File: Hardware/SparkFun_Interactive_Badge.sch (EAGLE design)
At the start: 1 part

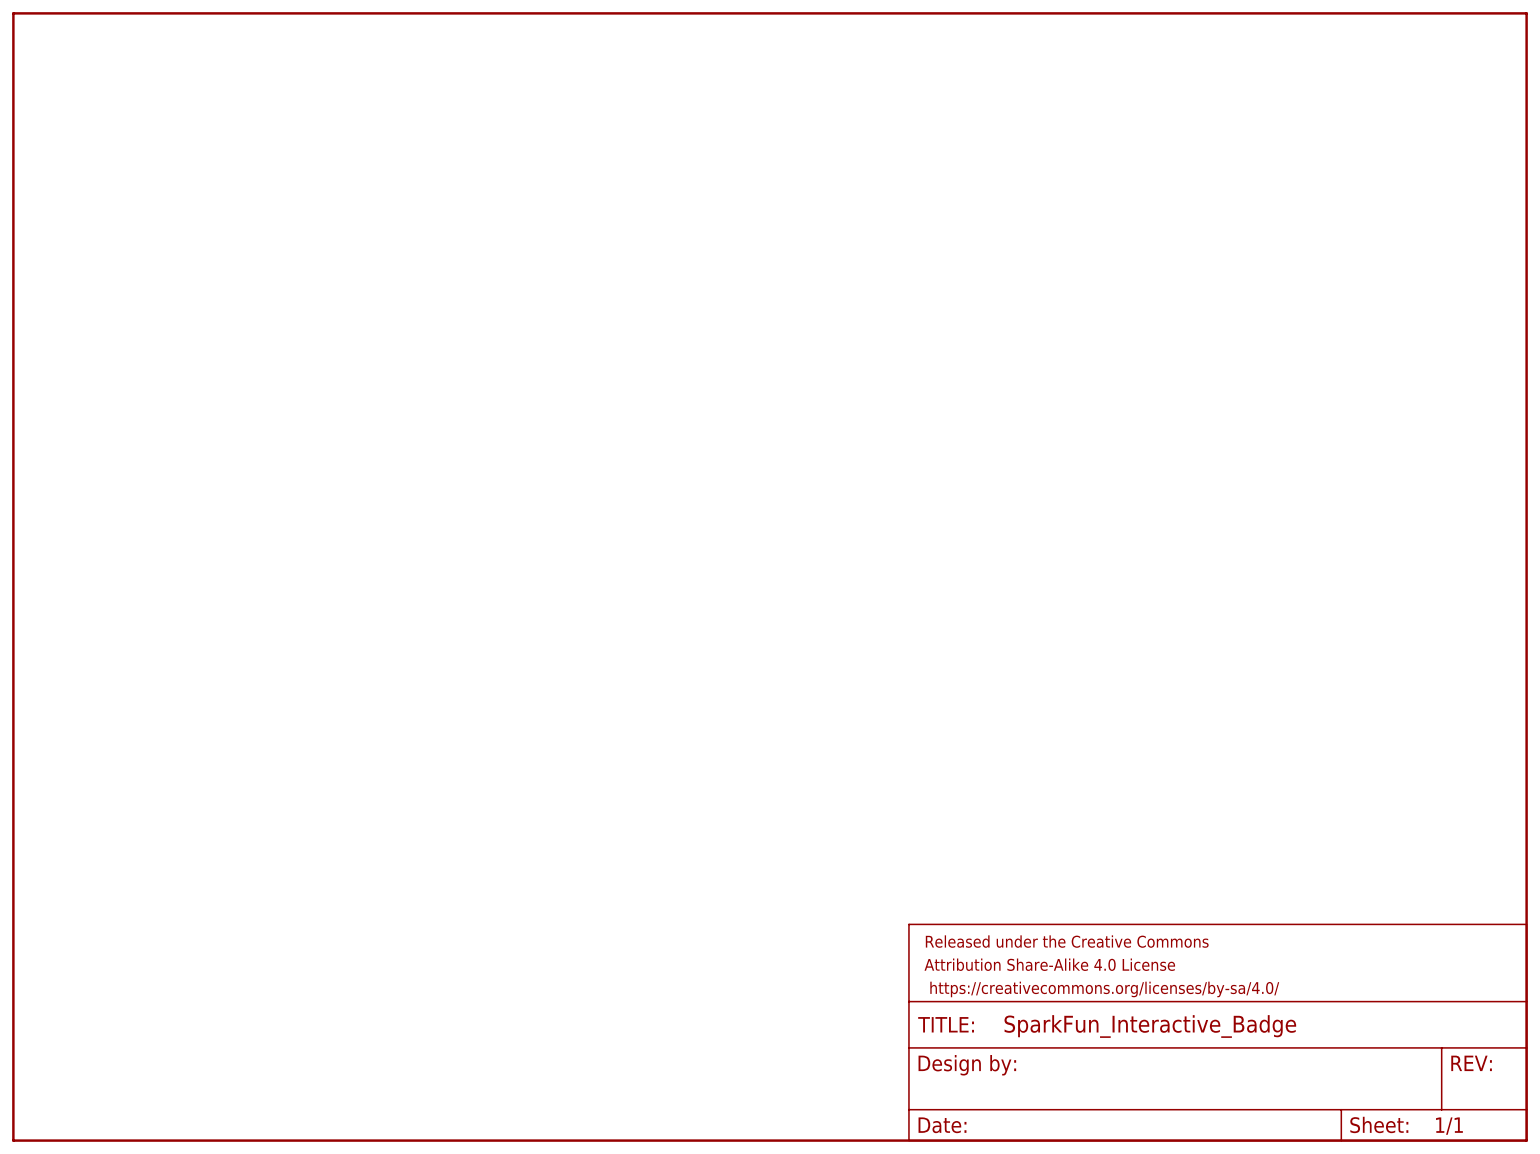
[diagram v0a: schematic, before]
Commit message: Started schematic. Voltage selection circuit added.
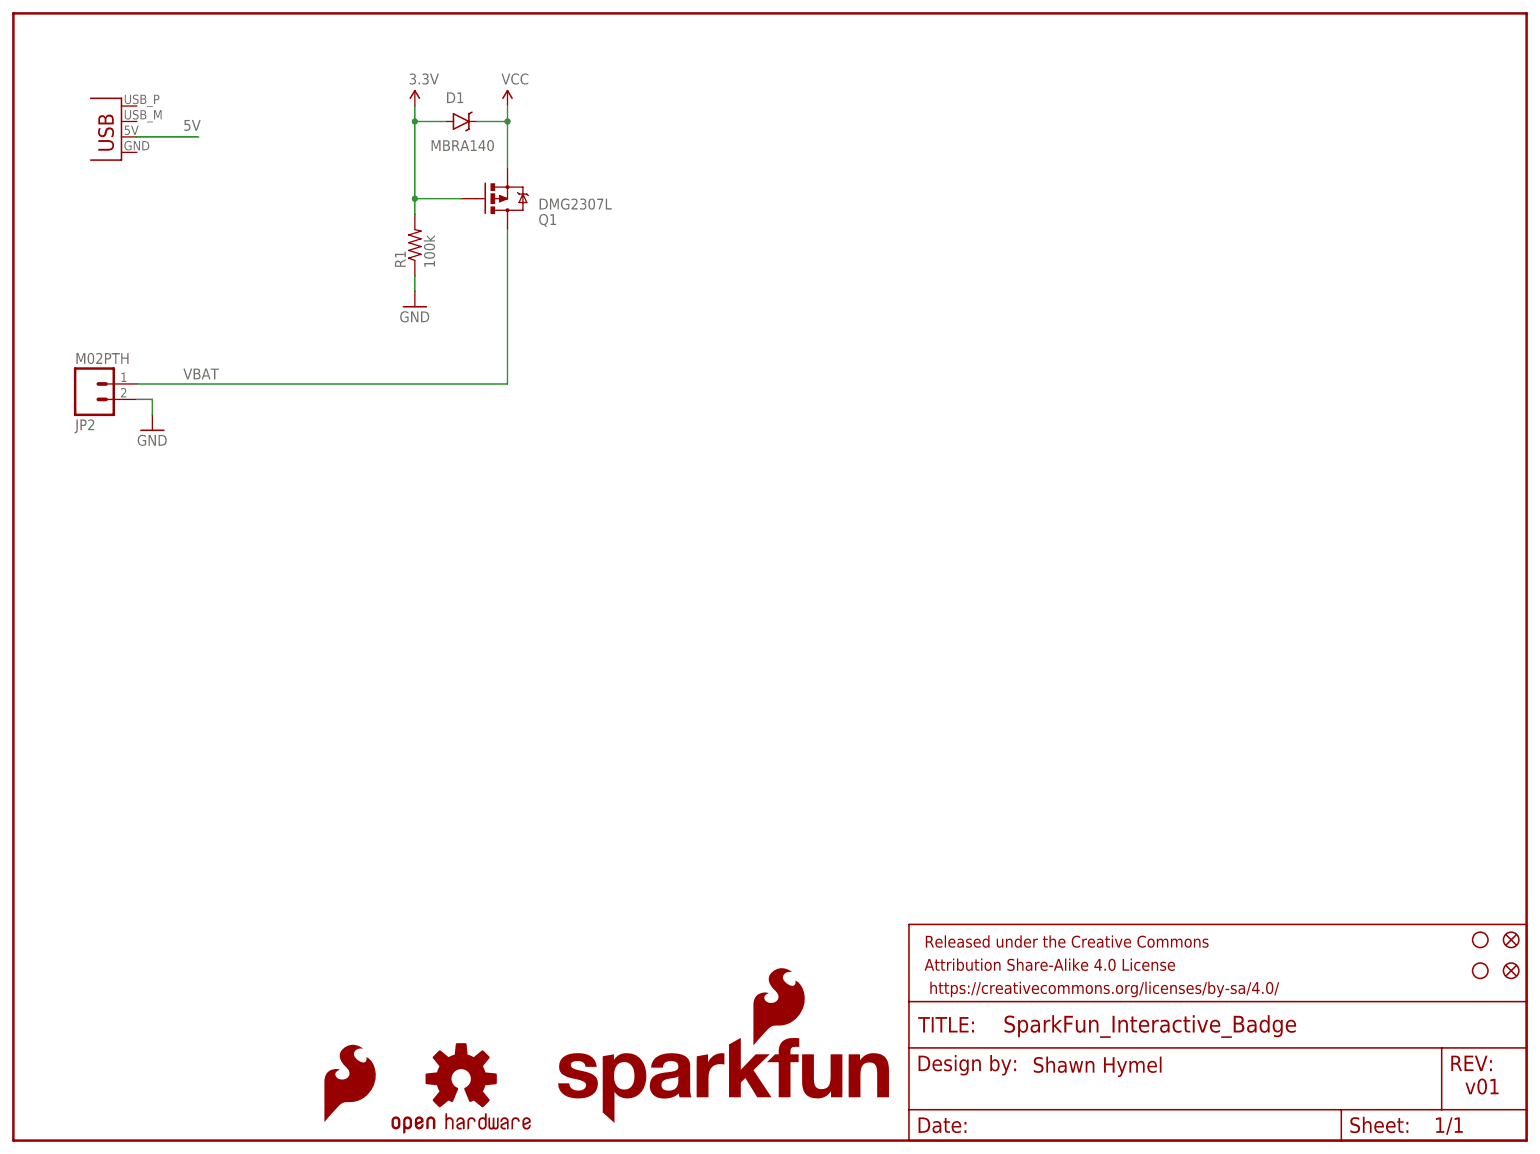
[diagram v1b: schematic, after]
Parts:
- added D1: MBRA140, SparkFun-DiscreteSemi:DIODE-SCHOTTKY-MBRA140
- added FID1, FID2: FIDUCIAL1X2, SparkFun-Aesthetics:FIDUCIAL1X2
- added JP1: USBPCB, SparkFun-Connectors:USBPCB
- added JP2: M02PTH, SparkFun-Connectors:M02PTH
- added LOGO1: SFE_LOGO_FLAME.1_INCH, SparkFun-Aesthetics:SFE_LOGO_FLAME.1_INCH
- added LOGO2: OSHW-LOGOS, SparkFun-Aesthetics:OSHW-LOGOS
- added Q1: DMG2307L, SparkFun-DiscreteSemi:MOSFET-PCHANNELDMG2307L
- added R1: 100k, SparkFun-Resistors:100KOHM1/10W1%(0603)
- added STANDOFF1, STANDOFF2: STAND-OFF, SparkFun-Electromechanical:STAND-OFF
- added U$1: SFE_LOGO_NAME_FLAME.1_INCH, SparkFun-Aesthetics:SFE_LOGO_NAME_FLAME.1_INCH
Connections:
- new net 3.3V: D1.A, Q1.G, R1.2
- new net 5V: JP1.VBUS
- new net GND: JP2.2, R1.1
- new net VBAT: JP2.1, Q1.D
- new net VCC: D1.C, Q1.S
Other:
- note added: "Shawn Hymel"
- note added: "v01"
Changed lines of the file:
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@@
 <setting verticaltext="up"/>
 </settings>
-<grid distance="0.1" unitdist="inch" unit="inch" style="lines" multiple="1" display="no" altdistance="0.01" altunitdist="inch" altunit="inch"/>
+<grid distance="0.1" unitdist="inch" unit="inch" style="lines" multiple="1" display="yes" altdistance="0.01" altunitdist="inch" altunit="inch"/>
 <layers>
 <layer number="1" name="Top" color="4" fill="1" visible="no" active="no"/>
@@
 <layer number="54" name="bGND_GNDA" color="1" fill="9" visible="no" active="no"/>
 <layer number="56" name="wert" color="7" fill="1" visible="no" active="no"/>
+<layer number="57" name="tCAD" color="7" fill="1" visible="no" active="no"/>
 <layer number="90" name="Modules" color="5" fill="1" visible="yes" active="yes"/>
 <layer number="91" name="Nets" color="2" fill="1" visible="yes" active="yes"/>
@@
 <layer number="97" name="Info" color="7" fill="1" visible="yes" active="yes"/>
 <layer number="98" name="Guide" color="6" fill="1" visible="yes" active="yes"/>
+<layer number="99" name="SpiceOrder" color="7" fill="1" visible="yes" active="yes"/>
 <layer number="100" name="Muster" color="7" fill="1" visible="no" active="no"/>
 <layer number="101" name="Patch_Top" color="12" fill="4" visible="yes" active="yes"/>
@@
 <layer number="108" name="tplace-old" color="10" fill="1" visible="no" active="yes"/>
 <layer number="109" name="ref-old" color="11" fill="1" visible="no" active="yes"/>
+<layer number="110" name="fp0" color="7" fill="1" visible="yes" active="yes"/>
+<layer number="111" name="LPC17xx" color="7" fill="1" visible="yes" active="yes"/>
+<layer number="112" name="tSilk" color="7" fill="1" visible="yes" active="yes"/>
+<layer number="113" name="IDFDebug" color="4" fill="1" visible="yes" active="yes"/>
 <layer number="116" name="Patch_BOT" color="9" fill="4" visible="yes" active="yes"/>
 <layer number="121" name="_tsilk" color="7" fill="1" visible="yes" active="yes"/>
 <layer number="122" name="_bsilk" color="7" fill="1" visible="yes" active="yes"/>
+<layer number="123" name="tTestmark" color="7" fill="1" visible="yes" active="yes"/>
+<layer number="124" name="bTestmark" color="7" fill="1" visible="yes" active="yes"/>
 <layer number="125" name="_tNames" color="7" fill="1" visible="yes" active="yes"/>
+<layer number="126" name="_bNames" color="7" fill="1" visible="yes" active="yes"/>
+<layer number="127" name="_tValues" color="7" fill="1" visible="yes" active="yes"/>
+<layer number="128" name="_bValues" color="7" fill="1" visible="yes" active="yes"/>
+<layer number="131" name="tAdjust" color="7" fill="1" visible="yes" active="yes"/>
+<layer number="132" name="bAdjust" color="7" fill="1" visible="yes" active="yes"/>
 <layer number="144" name="Drill_legend" color="7" fill="1" visible="yes" active="yes"/>
+<layer number="150" name="Notes" color="7" fill="1" visible="yes" active="yes"/>
 <layer number="151" name="HeatSink" color="7" fill="1" visible="yes" active="yes"/>
+<layer number="152" name="_bDocu" color="7" fill="1" visible="yes" active="yes"/>
+<layer number="153" name="FabDoc1" color="7" fill="1" visible="yes" active="yes"/>
+<layer number="154" name="FabDoc2" color="7" fill="1" visible="yes" active="yes"/>
+<layer number="155" name="FabDoc3" color="7" fill="1" visible="yes" active="yes"/>
 <layer number="199" name="Contour" color="7" fill="1" visible="yes" active="yes"/>
 <layer number="200" name="200bmp" color="1" fill="10" visible="yes" active="yes"/>
@@
 <layer number="223" name="223bmp" color="24" fill="1" visible="no" active="no"/>
 <layer number="224" name="224bmp" color="25" fill="1" visible="no" active="no"/>
+<layer number="248" name="Housing" color="7" fill="1" visible="yes" active="yes"/>
+<layer number="249" name="Edge" color="7" fill="1" visible="yes" active="yes"/>
 <layer number="250" name="Descript" color="3" fill="1" visible="no" active="no"/>
 <layer number="251" name="SMDround" color="12" fill="11" visible="no" active="no"/>
 <layer number="254" name="cooling" color="7" fill="1" visible="yes" active="yes"/>
+<layer number="255" name="routoute" color="7" fill="1" visible="no" active="yes"/>
 </layers>
 <schematic xreflabel="%F%N/%S" xrefpart="1_/%S.%C%R">
@@
 <parts>
 <part name="FRAME1" library="SparkFun-Aesthetics" deviceset="FRAME-LETTER" device=""/>
+<part name="FID1" library="SparkFun-Aesthetics" deviceset="FIDUCIAL" device="1X2"/>
+<part name="FID2" library="SparkFun-Aesthetics" deviceset="FIDUCIAL" device="1X2"/>
+<part name="STANDOFF1" library="SparkFun-Electromechanical" deviceset="STAND-OFF" device=""/>
+<part name="STANDOFF2" library="SparkFun-Electromechanical" deviceset="STAND-OFF" device=""/>
+<part name="LOGO1" library="SparkFun-Aesthetics" deviceset="SFE_LOGO_FLAME" device=".1_INCH"/>
+<part name="LOGO2" library="SparkFun-Aesthetics" deviceset="OSHW-LOGO" device="S"/>
+<part name="U$1" library="SparkFun-Aesthetics" deviceset="SFE_LOGO_NAME_FLAME" device=".1_INCH"/>
+<part name="JP1" library="SparkFun-Connectors" deviceset="USB" device="PCB"/>
+<part name="Q1" library="SparkFun-DiscreteSemi" deviceset="MOSFET-PCHANNEL" device="DMG2307L" value="DMG2307L"/>
+<part name="R1" library="SparkFun-Resistors" deviceset="100KOHM1/10W1%(0603)" device="" value="100k"/>
+<part name="D1" library="SparkFun-DiscreteSemi" deviceset="DIODE-SCHOTTKY" device="-MBRA140" value="MBRA140"/>
+<part name="GND15" library="SparkFun-Aesthetics" deviceset="GND" device=""/>
+<part name="SUPPLY1" library="SparkFun-Aesthetics" deviceset="VCC" device=""/>
+<part name="JP2" library="SparkFun-Connectors" deviceset="M02" device="PTH"/>
+<part name="GND1" library="SparkFun-Aesthetics" deviceset="GND" device=""/>
+<part name="SUPPLY2" library="SparkFun-Aesthetics" deviceset="3.3V" device=""/>
 </parts>
 <sheets>
 <sheet>
 <plain>
+<text x="238.76" y="7.62" size="2.54" layer="94">v01</text>
+<text x="167.64" y="11.176" size="2.54" layer="94">Shawn Hymel</text>
 </plain>
 <instances>
 <instance part="FRAME1" gate="G$1" x="0" y="0"/>
 <instance part="FRAME1" gate="G$2" x="147.32" y="0"/>
+<instance part="FID1" gate="G$1" x="246.38" y="33.02"/>
+<instance part="FID2" gate="G$1" x="246.38" y="27.94"/>
+<instance part="STANDOFF1" gate="G$1" x="241.3" y="33.02"/>
+<instance part="STANDOFF2" gate="G$1" x="241.3" y="27.94"/>
+<instance part="LOGO1" gate="G$1" x="50.8" y="2.54"/>
+<instance part="LOGO2" gate="G$1" x="73.66" y="10.16"/>
+<instance part="U$1" gate="G$1" x="88.9" y="2.54"/>
+<instance part="JP1" gate="G$1" x="17.78" y="162.56" rot="MR0"/>
+<instance part="Q1" gate="G$1" x="81.28" y="154.94" rot="MR180"/>
+<instance part="R1" gate="G$1" x="66.04" y="147.32" rot="R90"/>
+<instance part="D1" gate="G$1" x="73.66" y="167.64" smashed="yes">
+<attribute name="NAME" x="71.12" y="170.6626" size="1.778" layer="95"/>
+<attribute name="VALUE" x="68.58" y="162.7886" size="1.778" layer="96"/>
+</instance>
+<instance part="GND15" gate="1" x="66.04" y="137.16"/>
+<instance part="SUPPLY1" gate="G$1" x="81.28" y="170.18"/>
+<instance part="JP2" gate="G$1" x="12.7" y="124.46" rot="MR180"/>
+<instance part="GND1" gate="1" x="22.86" y="116.84"/>
+<instance part="SUPPLY2" gate="G$1" x="66.04" y="170.18"/>
 </instances>
 <busses>
 </busses>
 <nets>
+<net name="GND" class="0">
+<segment>
+<pinref part="R1" gate="G$1" pin="1"/>
+<pinref part="GND15" gate="1" pin="GND"/>
+<wire x1="66.04" y1="142.24" x2="66.04" y2="139.7" width="0.1524" layer="91"/>
+</segment>
+<segment>
+<pinref part="JP2" gate="G$1" pin="2"/>
+<wire x1="20.32" y1="121.92" x2="22.86" y2="121.92" width="0.1524" layer="91"/>
+<pinref part="GND1" gate="1" pin="GND"/>
+<wire x1="22.86" y1="121.92" x2="22.86" y2="119.38" width="0.1524" layer="91"/>
+</segment>
+</net>
+<net name="VBAT" class="0">
+<segment>
+<pinref part="Q1" gate="G$1" pin="D"/>
+<wire x1="20.32" y1="124.46" x2="81.28" y2="124.46" width="0.1524" layer="91"/>
+<wire x1="81.28" y1="124.46" x2="81.28" y2="149.86" width="0.1524" layer="91"/>
+<pinref part="JP2" gate="G$1" pin="1"/>
+<label x="27.94" y="125.222" size="1.778" layer="95"/>
+</segment>
+</net>
+<net name="VCC" class="0">
+<segment>
+<pinref part="D1" gate="G$1" pin="C"/>
+<wire x1="76.2" y1="167.64" x2="81.28" y2="167.64" width="0.1524" layer="91"/>
+<wire x1="81.28" y1="167.64" x2="81.28" y2="170.18" width="0.1524" layer="91"/>
+<pinref part="Q1" gate="G$1" pin="S"/>
+<wire x1="81.28" y1="167.64" x2="81.28" y2="160.02" width="0.1524" layer="91"/>
+<junction x="81.28" y="167.64"/>
+<pinref part="SUPPLY1" gate="G$1" pin="VCC"/>
+</segment>
+</net>
+<net name="3.3V" class="0">
+<segment>
+<pinref part="D1" gate="G$1" pin="A"/>
+<pinref part="R1" gate="G$1" pin="2"/>
+<wire x1="66.04" y1="167.64" x2="71.12" y2="167.64" width="0.1524" layer="91"/>
+<wire x1="66.04" y1="152.4" x2="66.04" y2="154.94" width="0.1524" layer="91"/>
+<pinref part="Q1" gate="G$1" pin="G"/>
+<wire x1="66.04" y1="154.94" x2="66.04" y2="167.64" width="0.1524" layer="91"/>
+<wire x1="73.66" y1="154.94" x2="66.04" y2="154.94" width="0.1524" layer="91"/>
+<junction x="66.04" y="154.94"/>
+<wire x1="66.04" y1="167.64" x2="66.04" y2="170.18" width="0.1524" layer="91"/>
+<junction x="66.04" y="167.64"/>
+<pinref part="SUPPLY2" gate="G$1" pin="3.3V"/>
+</segment>
+</net>
+<net name="5V" class="0">
+<segment>
+<pinref part="JP1" gate="G$1" pin="VBUS"/>
+<wire x1="20.32" y1="165.1" x2="30.48" y2="165.1" width="0.1524" layer="91"/>
+<label x="27.94" y="166.116" size="1.778" layer="95"/>
+</segment>
+</net>
 </nets>
 </sheet>

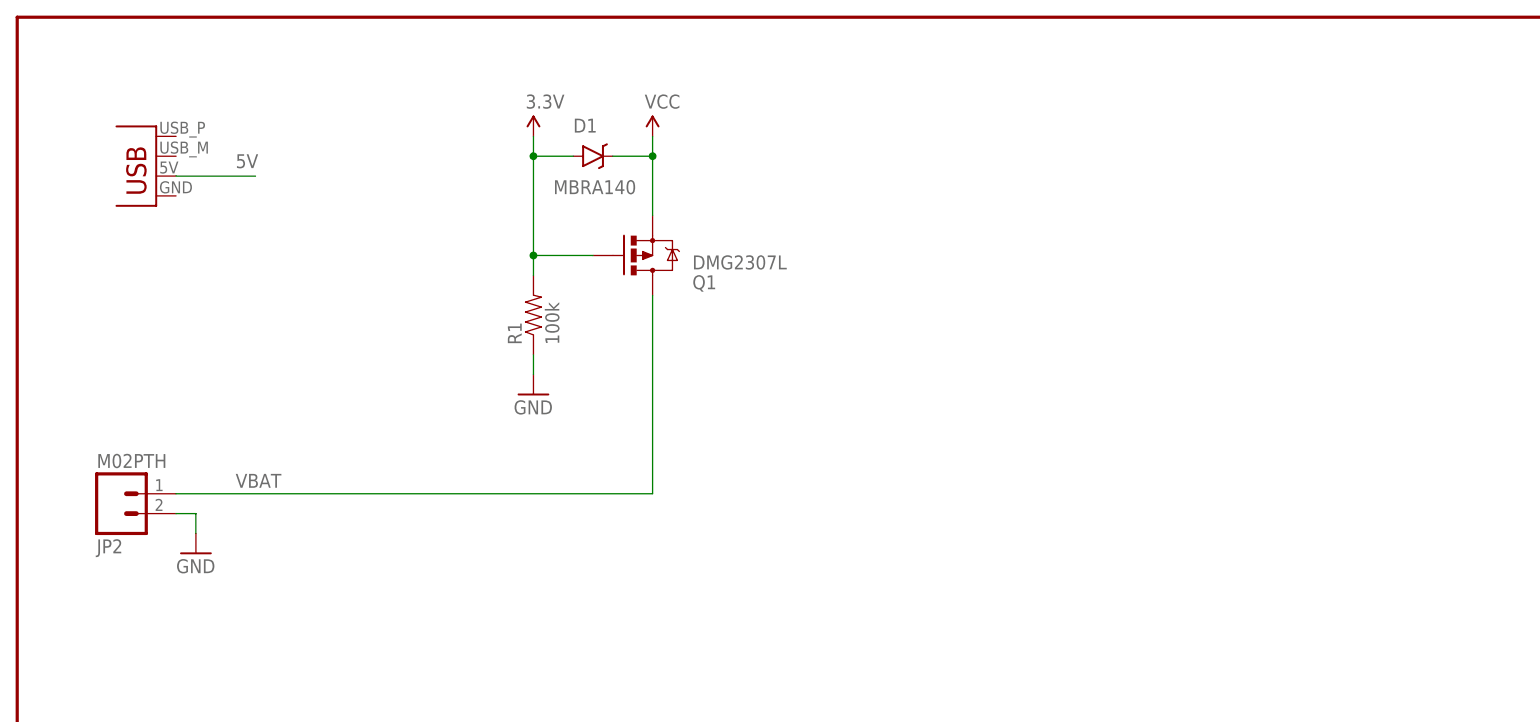
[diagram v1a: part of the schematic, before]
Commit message: Added LDO to power section in sch
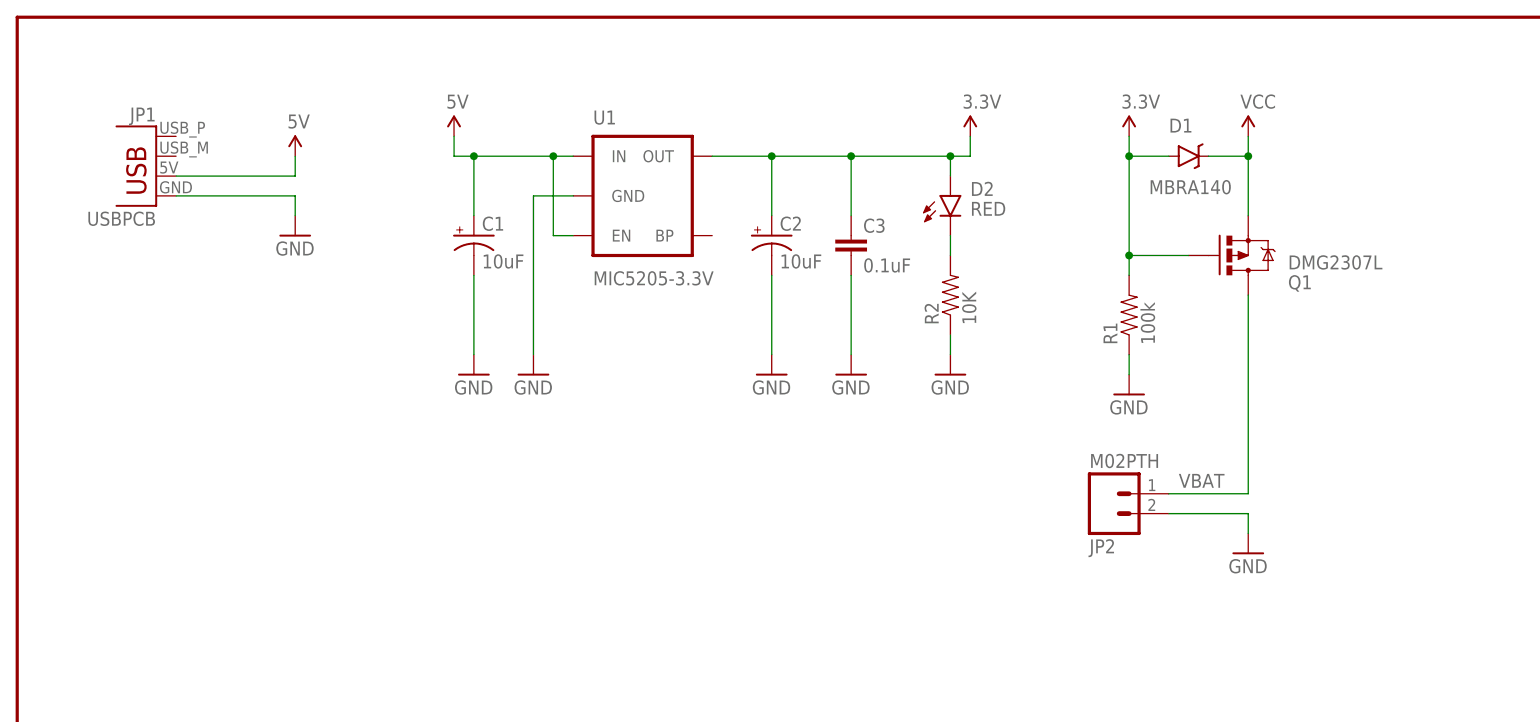
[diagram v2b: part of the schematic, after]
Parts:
- added C1, C2: 10uF, SparkFun-Capacitors:10UF-16V-10%(TANT)
- added C3: 0.1uF, SparkFun-Capacitors:0.1UF-25V(+80/-20%)(0603)
- added D2: RED, SparkFun-LED:LED-RED0603
- added R2: 10K, SparkFun-Resistors:10KOHM-1/10W-1%(0603)0603
- added U1: MIC5205-3.3V, SparkFun-PowerIC:MIC52053.3V
- R1: device SparkFun-Resistors:100KOHM1/10W1%(0603) -> SparkFun-Resistors:100KOHM-1/10W-1%(0603)
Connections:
- new net N$4: D2.C, R2.2
- net 3.3V: now also C2.+, C3.1, D2.A, U1.OUT
- net 5V: now also C1.+, U1.EN, U1.IN
- net GND: now also C1.-, C2.-, C3.2, JP1.GND, R2.1, U1.GND
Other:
- moved on the sheet: D1, JP2, Q1, R1
